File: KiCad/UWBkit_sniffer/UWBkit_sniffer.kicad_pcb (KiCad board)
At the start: 4 copper layers, 57.4 x 57.4 mm, 78 parts, among them J1 Conn_Coaxial, J10 Conn_SPIM, J11 Conn_01x02, J2 Conn_SWD, J3 Conn_GPIO, J4 Conn_01x04, J5 Conn_I2C2, J6 USB_C_Receptacle_USB2.0_14P, J7 USB_C_Receptacle_USB2.0_14P, J8 Conn_SPIS, J9 Conn_I2C1, SW1 SW_Push, SW2 SW_Slide_DPDT, U1 LBUA5QJ2AB, U2 CP2104, U4 XC9285B33CMR-G, U5 IP4234CZ6, U6 IP4234CZ6

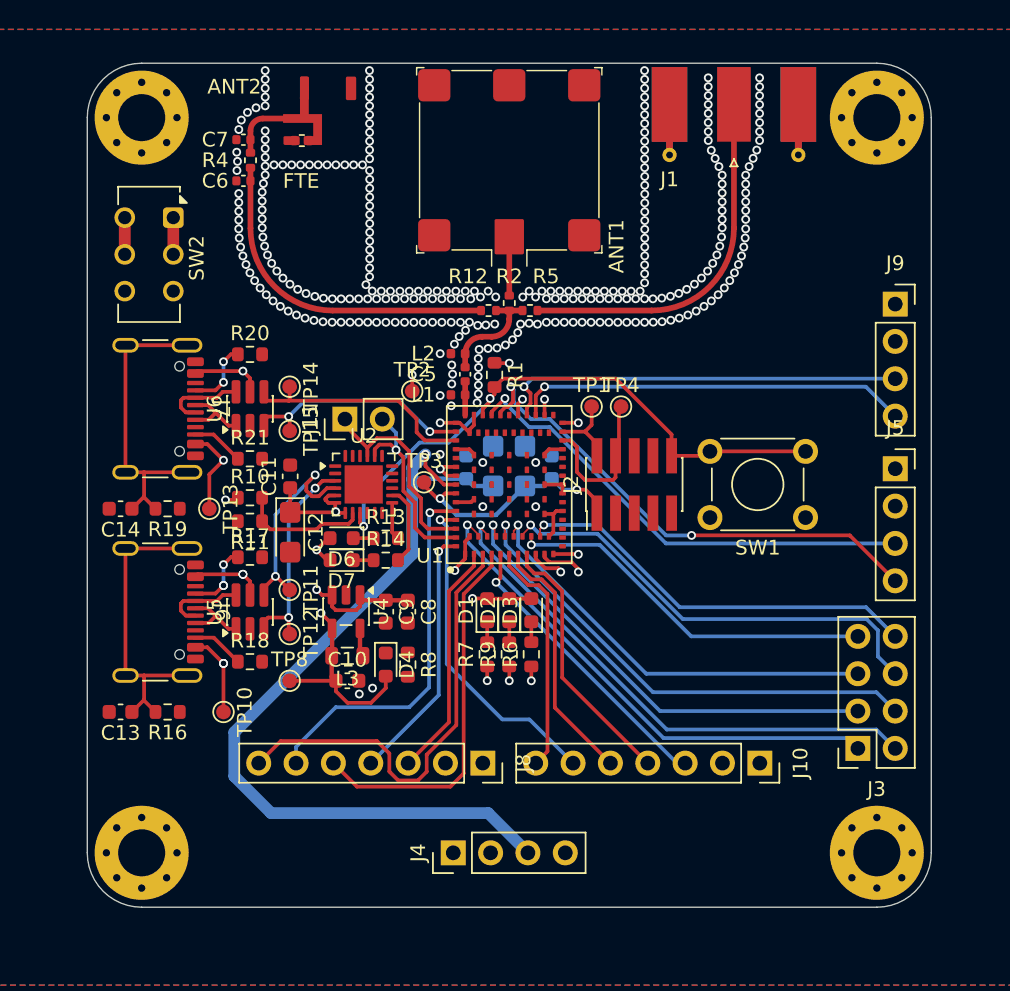
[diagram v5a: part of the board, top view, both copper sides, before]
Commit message: United 5V rails, modified layout of connectors
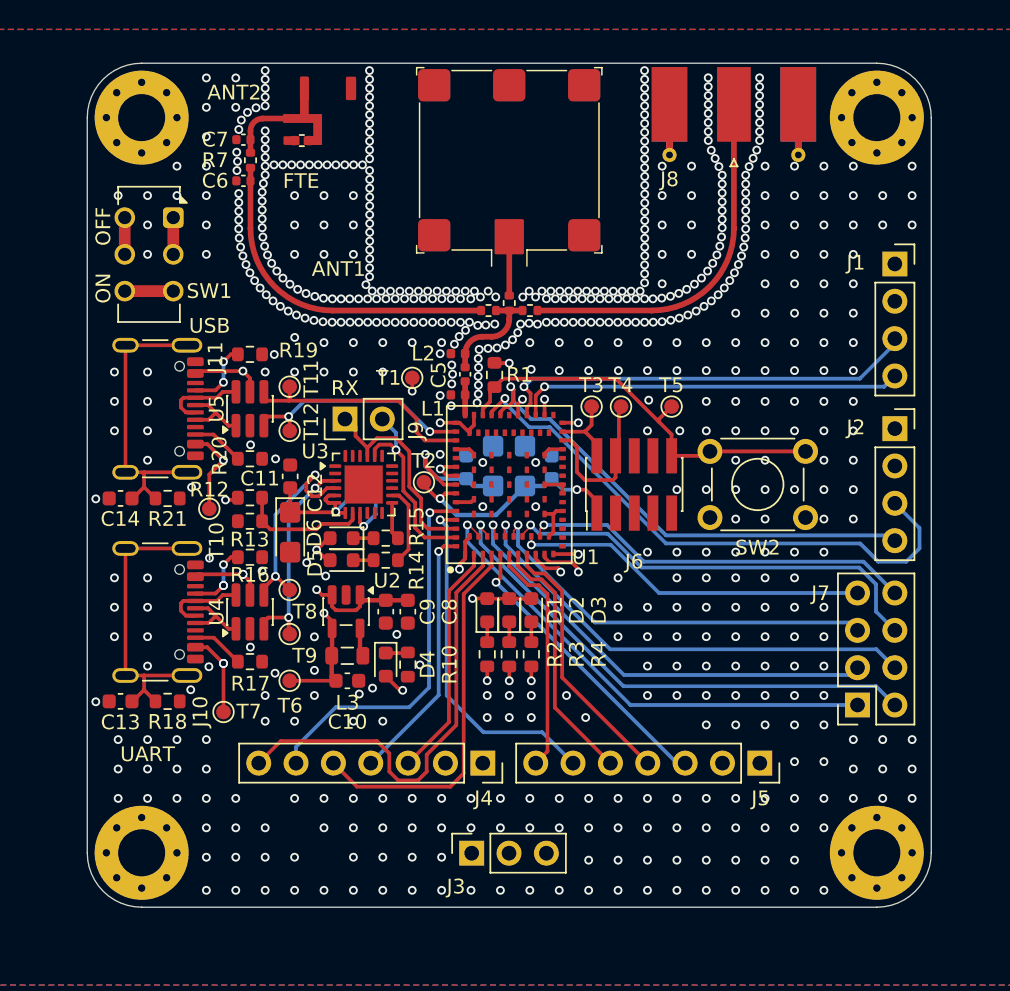
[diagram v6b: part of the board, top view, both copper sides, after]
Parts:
- removed D7: R, LED_SMD:LED_0603_1608Metric
- removed the J4 at (156.8, 109.7)
- removed TP1, TP10, TP11, TP12, TP13, TP14, TP15, TP2, TP3, TP4, TP8: TestPoint_Small, TestPoint:TestPoint_Pad_D1.0mm
- removed U6: IP4234CZ6, Package_TO_SOT_SMD:SC-74-6_1.55x2.9mm_P0.95mm
- added D5: R, LED_SMD:LED_0603_1608Metric, F.Cu at (149.2, 89.8)
- added J3: Conn_01x03, Connector_PinSocket_2.54mm:PinSocket_1x03_P2.54mm_Vertical, F.Cu at (158.0, 109.7)
- added R11: 100k, Resistor_SMD:R_0603_1608Metric, B.Cu at (150.7, 84.7)
- added T1: TestPoint_Small, TestPoint:TestPoint_Pad_D1.0mm, F.Cu at (154.0, 77.4)
- added T10: TestPoint_Small, TestPoint:TestPoint_Pad_D1.0mm, F.Cu at (140.2, 86.3)
- added T11: TestPoint_Small, TestPoint:TestPoint_Pad_D1.0mm, F.Cu at (145.7, 78.0)
- added T12: TestPoint_Small, TestPoint:TestPoint_Pad_D1.0mm, F.Cu at (145.7, 81.0)
- added T2: TestPoint_Small, TestPoint:TestPoint_Pad_D1.0mm, F.Cu at (154.8, 84.5)
- added T3: TestPoint_Small, TestPoint:TestPoint_Pad_D1.0mm, F.Cu at (166.2, 79.3)
- added T4: TestPoint_Small, TestPoint:TestPoint_Pad_D1.0mm, F.Cu at (168.2, 79.3)
- added T5: TestPoint_Small, TestPoint:TestPoint_Pad_D1.0mm, F.Cu at (171.6, 79.3)
- added T6: TestPoint_Small, TestPoint:TestPoint_Pad_D1.0mm, F.Cu at (145.7, 98.0)
- added T7: TestPoint_Small, TestPoint:TestPoint_Pad_D1.0mm, F.Cu at (141.2, 100.1)
- added T8: TestPoint_Small, TestPoint:TestPoint_Pad_D1.0mm, F.Cu at (145.7, 91.8)
- added T9: TestPoint_Small, TestPoint:TestPoint_Pad_D1.0mm, F.Cu at (145.7, 94.8)
- added U5: IP4234CZ6, Package_TO_SOT_SMD:SC-74-6_1.55x2.9mm_P0.95mm, F.Cu at (143.0, 79.5)
- moved J7 2.95 mm to (184.3, 99.7)
- moved J2 2.73 mm to (186.8, 80.8)
- moved J1 2.73 mm to (186.8, 69.7)
- moved C13 0.72 mm to (134.2, 99.4)
- moved R18 0.72 mm to (137.4, 99.4)
- moved C14 0.70 mm to (134.2, 85.6)
- moved R21 0.70 mm to (137.4, 85.6)
- renumbered J9 to J1, J6 to J10, J7 to J11, J5 to J2, J8 to J4, J10 to J5, J2 to J6, J3 to J7, J1 to J8, J11 to J9, R8 to R10, R10 to R12, R11 to R13, R13 to R15, R17 to R16, R18 to R17, R16 to R18, R20 to R19, R7 to R2, R21 to R20, R19 to R21, R9 to R3, R6 to R4, R2 to R5, R12 to R6, R4 to R7, R3 to R8, R5 to R9, SW2 to SW1, SW1 to SW2, U4 to U2, U2 to U3, U5 to U4
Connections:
- C8 pad 1: +5V -> SOC_VBUS
- C9 pad 1: +5V -> SOC_VBUS
- J6 pad 10: /nRST -> /CPU/nRST
- R1 pad 2: /nRST -> /CPU/nRST
- R12 pad 1: +5V -> SOC_VBUS
- SW1 pad 4: +5V -> SOC_VBUS
- SW2 pad 2: /nRST -> /CPU/nRST
- U1 pad 35: /nRST -> /CPU/nRST
- U2 pad 1: +5V -> SOC_VBUS
- U2 pad 3: +5V -> SOC_VBUS
- U3 pad 9: /nRST -> Net-(U3-~{RST})
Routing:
- net +5V: track 73.2 -> 0.00 mm, vias 2 -> 0
- net /nRST: track 41.2 -> 0.00 mm, vias 2 -> 0
- net /CPU/nRST: track 0.00 -> 28.1 mm
- net SOC_VBUS: track 84.5 -> 112.3 mm, vias 2 -> 4
- net /CPU/I2C2_SCL: track 32.3 -> 38.8 mm
- net Net-(U3-~{RST}): track 0.00 -> 4.21 mm, vias 0 -> 1
- net +3V3: track 162.6 -> 165.2 mm, vias 8 -> 9
- net Net-(D4-K): track 0.00 -> 1.52 mm
- net /CPU/I2C1_SCL: track 27.7 -> 29.0 mm
- net /CPU/SPIM_RESET: track 22.4 -> 23.7 mm
- net Net-(J7-Pin_8): track 27.9 -> 26.7 mm
- net Net-(J7-Pin_7): track 25.4 -> 24.1 mm
- net Net-(J7-Pin_5): track 29.0 -> 27.8 mm
- net Net-(J7-Pin_4): track 33.3 -> 32.1 mm
- net Net-(J7-Pin_1): track 34.7 -> 33.4 mm
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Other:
- board text added: "OFF"
- board text added: "ON"
- board text added: "RX"
- board text added: "UART"
- board text added: "USB"

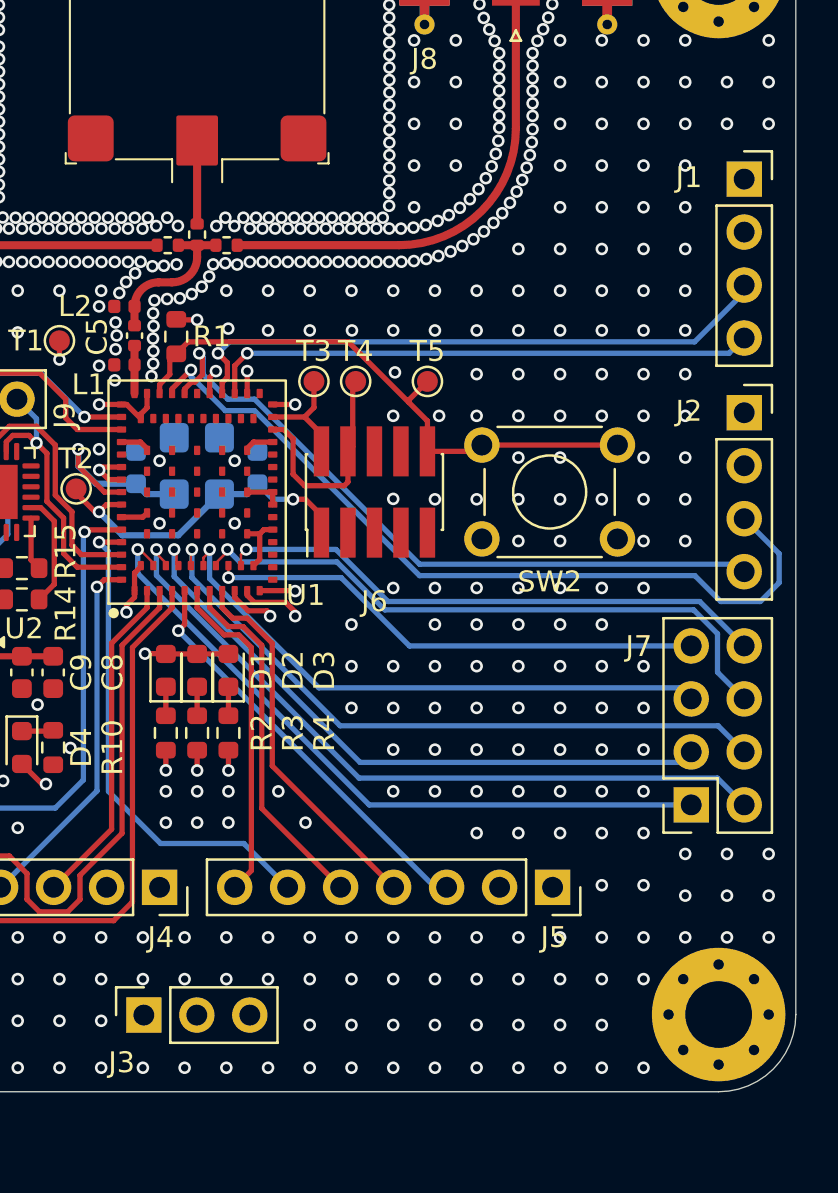
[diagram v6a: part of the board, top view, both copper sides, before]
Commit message: Added placeholder silkscreen elements
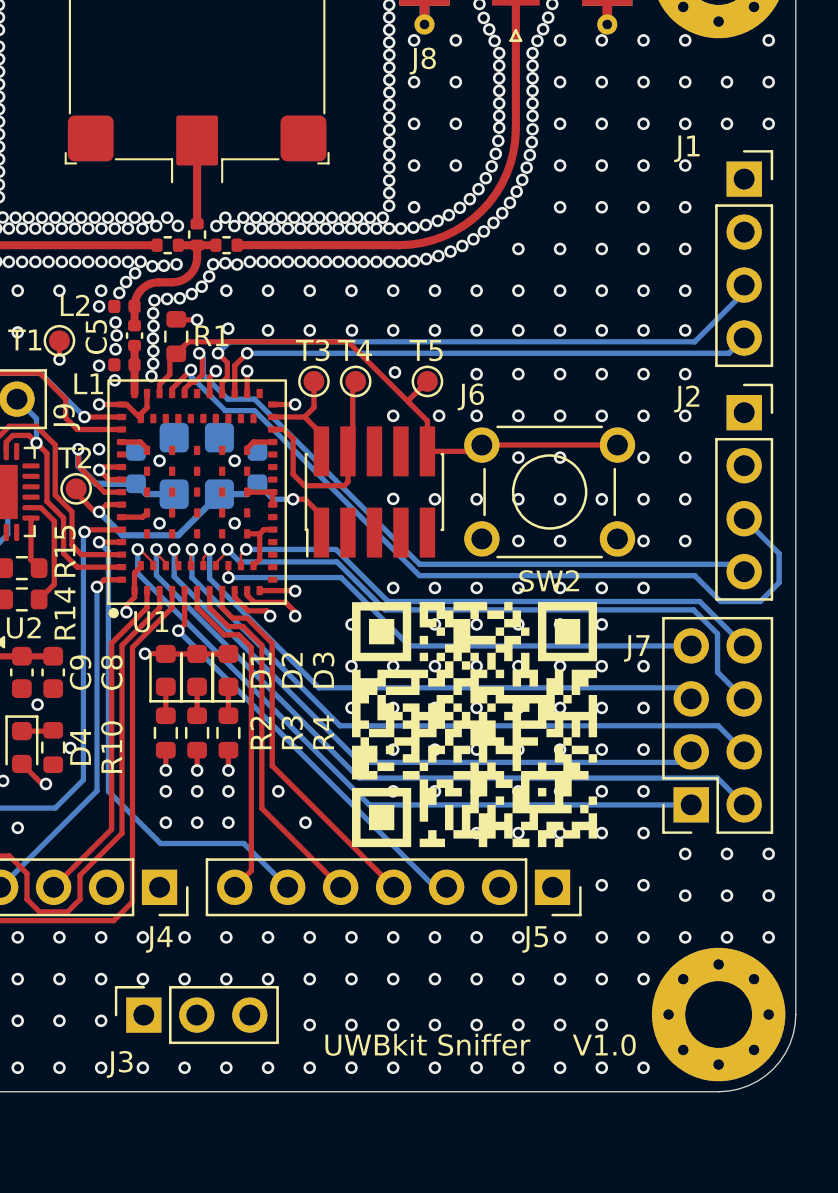
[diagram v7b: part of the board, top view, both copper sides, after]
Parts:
- added QR*****: https://github.com/GraniteGobbler/UWBkit, UWBkit:Git-Repo-QR, F.Cu at (173.9, 95.8)
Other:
- board text added: "UWBkit Sniffer"
- board text added: "V1.0"
